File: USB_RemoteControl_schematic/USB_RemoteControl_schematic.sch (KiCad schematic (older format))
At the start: 33 parts, among them J1 USB_A, J2 FOUR_WIRE_CONN, SW1 ~rst, SW2 boot, U1 AMS1117-3.3, U2 STM32F103C6Tx, U3 NRF24L01_Breakout, Y1 8MHz

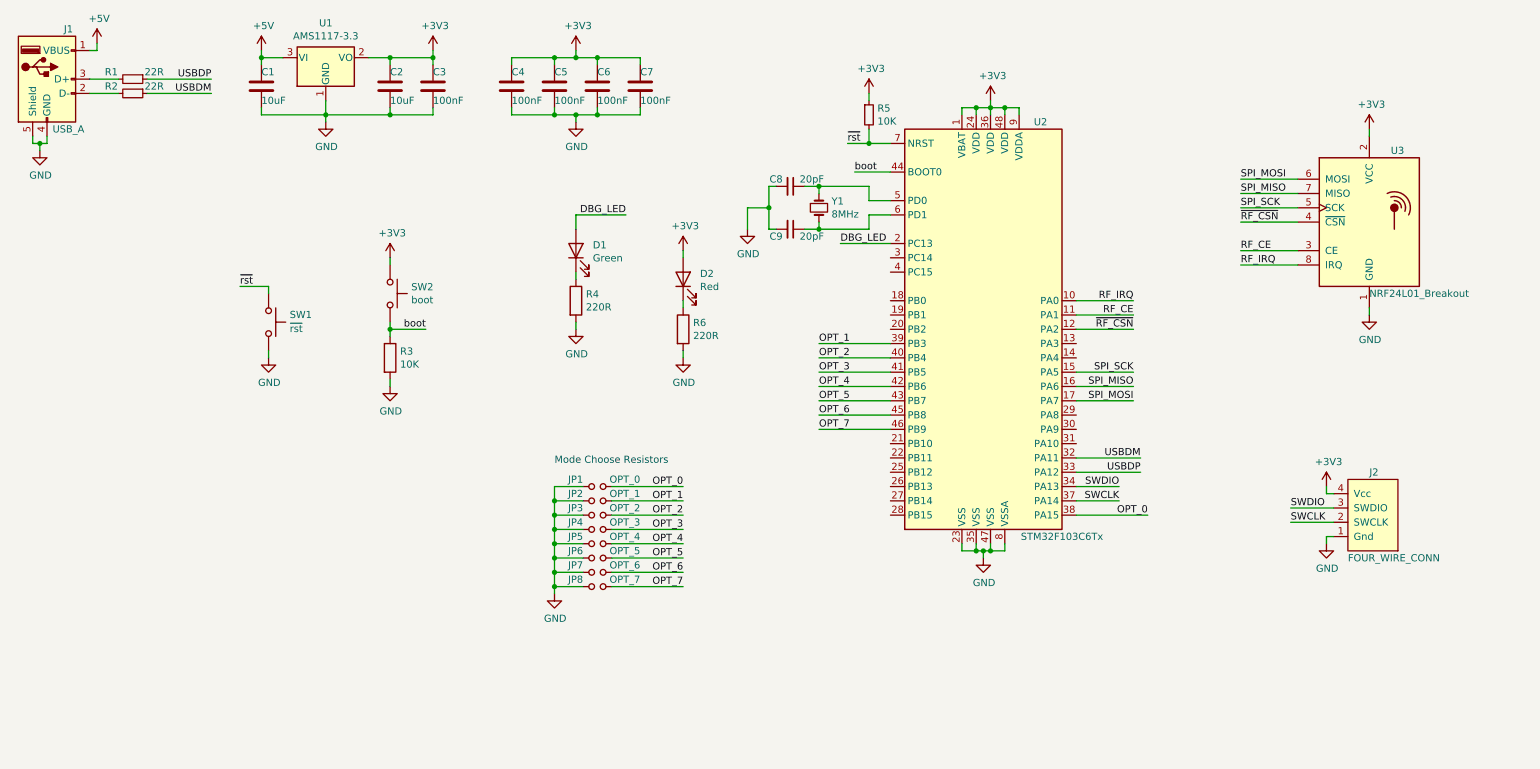
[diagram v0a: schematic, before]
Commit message: Completed schematic for Version02
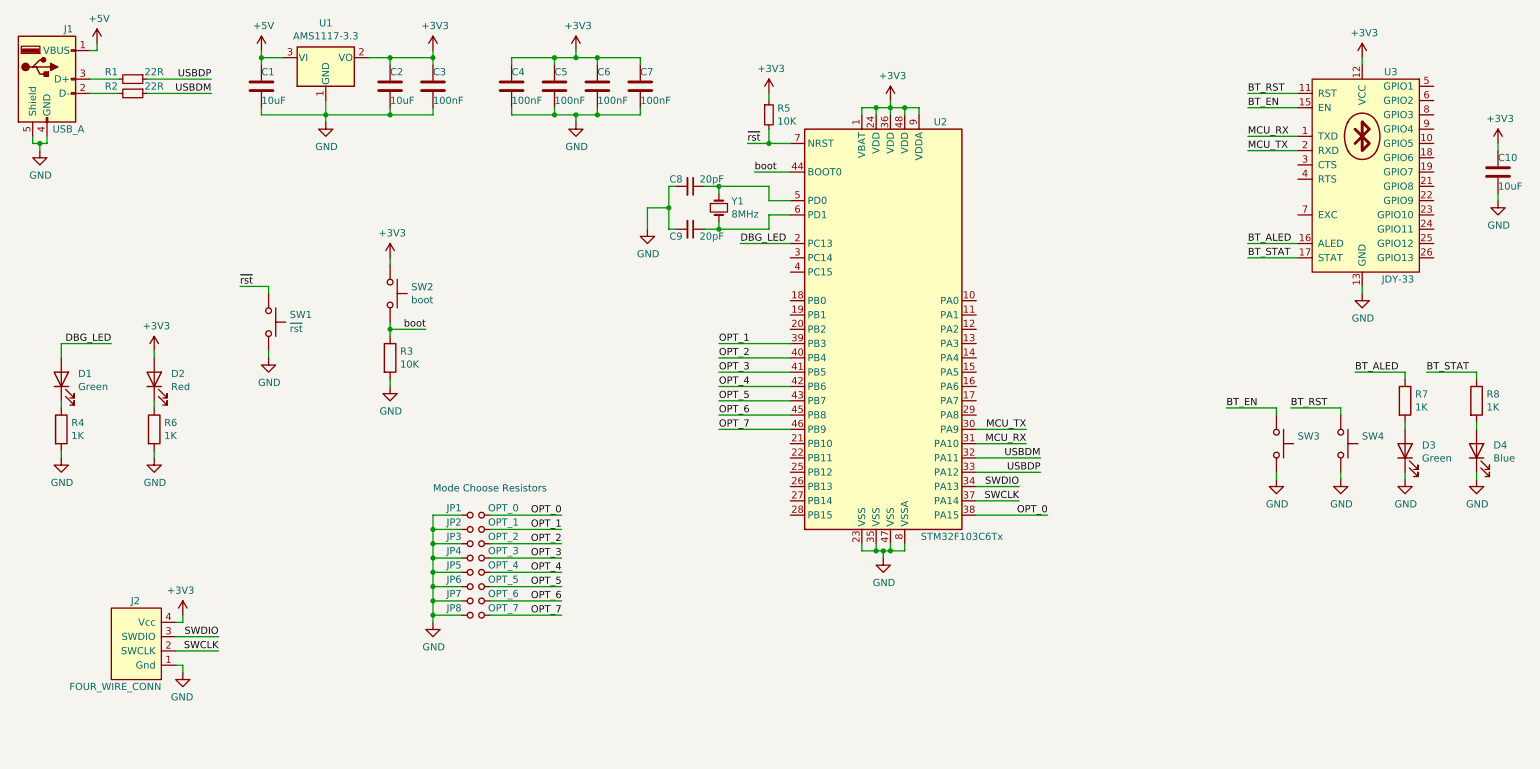
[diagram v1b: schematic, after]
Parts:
- removed U3: NRF24L01_Breakout, RF_Module:nRF24L01_Breakout, symbol RF:NRF24L01_Breakout
- added C10: 10uF, Capacitor_SMD:C_0805_2012Metric_Pad1.18x1.45mm_HandSolder, symbol Device:C
- added D3: Green, LED_SMD:LED_1206_3216Metric_Pad1.42x1.75mm_HandSolder, symbol Device:LED
- added D4: Blue, LED_SMD:LED_1206_3216Metric_Pad1.42x1.75mm_HandSolder, symbol Device:LED
- added R7, R8: 1K, Resistor_SMD:R_0805_2012Metric_Pad1.20x1.40mm_HandSolder, symbol Device:R
- added SW3, SW4: ~, custom_buttons_switches:TSB008, symbol Switch:SW_Push
- added U3: JDY-33, Bluetooth_Custom:JDY-33, JDY-32, JDY-31, JDY-30, JDY-09, symbol Bluetooth_Custom:JDY-33
- C1, C2: footprint Capacitor_SMD:C_1206_3216Metric_Pad1.33x1.80mm_HandSolder -> Capacitor_SMD:C_0805_2012Metric_Pad1.18x1.45mm_HandSolder
- C3, C4, C5, C6, C7: footprint Capacitor_SMD:C_0603_1608Metric_Pad1.08x0.95mm_HandSolder -> Capacitor_SMD:C_0805_2012Metric_Pad1.18x1.45mm_HandSolder
- J1: footprint Connector_USB:USB_A_CONNFLY_DS1095-WNR0 -> Connectors_Custom:USB_A_Male
- R4, R6: value 220R -> 1K
- Y1: footprint Crystal:Crystal_SMD_HC49-SD_HandSoldering -> Crystal:Crystal_SMD_HC49-SD
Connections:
- net +3V3: now also C10.1, U3.12 (VCC)
- net GND: now also C10.2, D3.1 (K), D4.1 (K), SW3.2, SW4.2, U3.13 (GND)
- net MCU_TX: now reaches U2.30 (PA9)
- net MCU_TX: now also U3.2 (RXD)
- net MCU_RX: now reaches U2.31 (PA10)
- net MCU_RX: now also U3.1 (TXD)
- net RF_CE: no longer names the net of U2.11 (PA1)
- net RF_IRQ: no longer names the net of U2.10 (PA0)
- net SPI_MISO: no longer names the net of U2.16 (PA6)
- net SPI_MOSI: no longer names the net of U2.17 (PA7)
- net SPI_SCK: no longer names the net of U2.15 (PA5)
- net ~RF_CSN: no longer names the net of U2.12 (PA2)
- new net: D3.2 (A), R7.2
- new net: D4.2 (A), R8.2
- new net BT_ALED: R7.1, U3.16 (ALED)
- new net BT_EN: SW3.1, U3.15 (EN)
- new net BT_RST: SW4.1, U3.11 (RST)
- new net BT_STAT: R8.1, U3.17 (STAT)
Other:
- moved on the sheet: C8, C9, D1, D2, J2, JP1, JP2, JP3, JP4, JP5, JP6, JP7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

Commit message: Finished PCB
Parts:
- removed C10: 10uF, Capacitor_SMD:C_0805_2012Metric_Pad1.18x1.45mm_HandSolder, symbol Device:C
- removed JP1: OPT_0, Resistor_SMD:R_0805_2012Metric_Pad1.20x1.40mm_HandSolder, symbol Device:Jumper_NO_Small
- removed JP2: OPT_1, Resistor_SMD:R_0805_2012Metric_Pad1.20x1.40mm_HandSolder, symbol Device:Jumper_NO_Small
- removed JP3: OPT_2, Resistor_SMD:R_0805_2012Metric_Pad1.20x1.40mm_HandSolder, symbol Device:Jumper_NO_Small
- removed JP4: OPT_3, Resistor_SMD:R_0805_2012Metric_Pad1.20x1.40mm_HandSolder, symbol Device:Jumper_NO_Small
- removed JP5: OPT_4, Resistor_SMD:R_0805_2012Metric_Pad1.20x1.40mm_HandSolder, symbol Device:Jumper_NO_Small
- removed JP6: OPT_5, Resistor_SMD:R_0805_2012Metric_Pad1.20x1.40mm_HandSolder, symbol Device:Jumper_NO_Small
- removed JP7: OPT_6, Resistor_SMD:R_0805_2012Metric_Pad1.20x1.40mm_HandSolder, symbol Device:Jumper_NO_Small
- removed JP8: OPT_7, Resistor_SMD:R_0805_2012Metric_Pad1.20x1.40mm_HandSolder, symbol Device:Jumper_NO_Small
- removed U1: AMS1117-3.3, Package_TO_SOT_SMD:SOT-223-3_TabPin2, symbol Regulator_Linear:AMS1117-3.3
- added U1: HT7533, Package_TO_SOT_SMD:SOT-89-3, symbol Regulator_Linear:HT75xx-1-SOT89
- C3, C4, C5, C6, C7: footprint Capacitor_SMD:C_0805_2012Metric_Pad1.18x1.45mm_HandSolder -> Capacitor_SMD:C_0603_1608Metric_Pad1.08x0.95mm_HandSolder
- D1, D2, D3, D4: footprint LED_SMD:LED_1206_3216Metric_Pad1.42x1.75mm_HandSolder -> LED_SMD:LED_0805_2012Metric_Pad1.15x1.40mm_HandSolder
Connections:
- net OPT_4 is gone; now on net MCU_TX: U2.42 (PB6)
- net OPT_5 is gone; now on net MCU_RX: U2.43 (PB7)
- net +3V3: now also R6.1, U1.3 (VOUT); no longer D2.2 (A)
- net +5V: now also U1.2 (VIN)
- net DBG_LED: now also R4.1, U2.10 (PA0); no longer D1.2 (A), U2.2 (PC13)
- net GND: now also D1.1 (K), D2.1 (K), U1.1 (GND); no longer R4.2, R6.2
- net MCU_RX: no longer U2.31 (PA10)
- net MCU_TX: no longer U2.30 (PA9)
- net OPT_0: no longer names the net of U2.38 (PA15)
- net OPT_1: no longer names the net of U2.39 (PB3)
- net OPT_2: no longer names the net of U2.40 (PB4)
- net OPT_3: no longer names the net of U2.41 (PB5)
- net OPT_6: no longer names the net of U2.45 (PB8)
- net OPT_7: no longer names the net of U2.46 (PB9)
- new net: D1.2 (A), R4.2
- new net: D2.2 (A), R6.2
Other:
- note removed: "Mode Choose Resistors"
- moved on the sheet: D1, D2, R4, R6

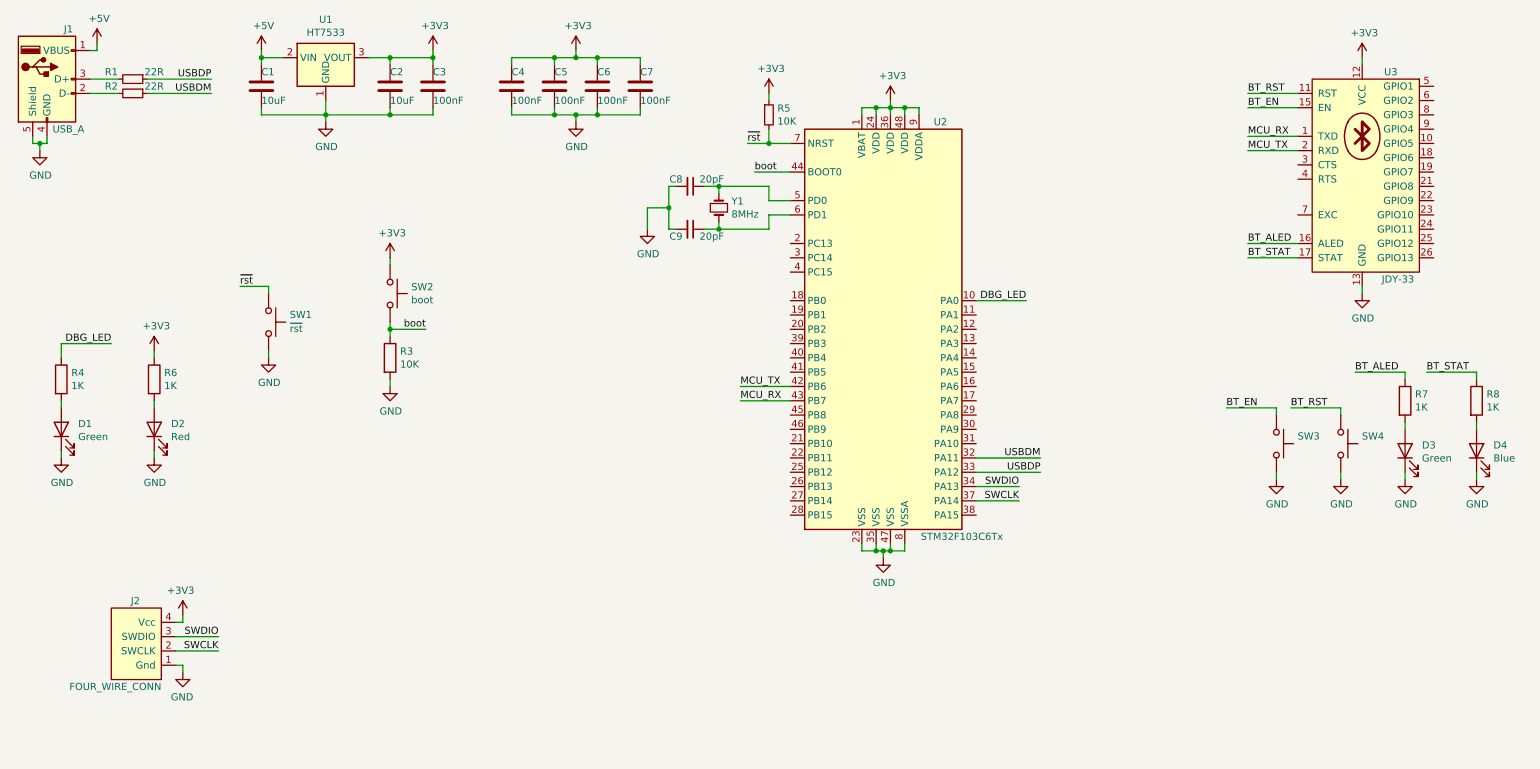
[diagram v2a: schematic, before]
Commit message: Improved readability of the schematic
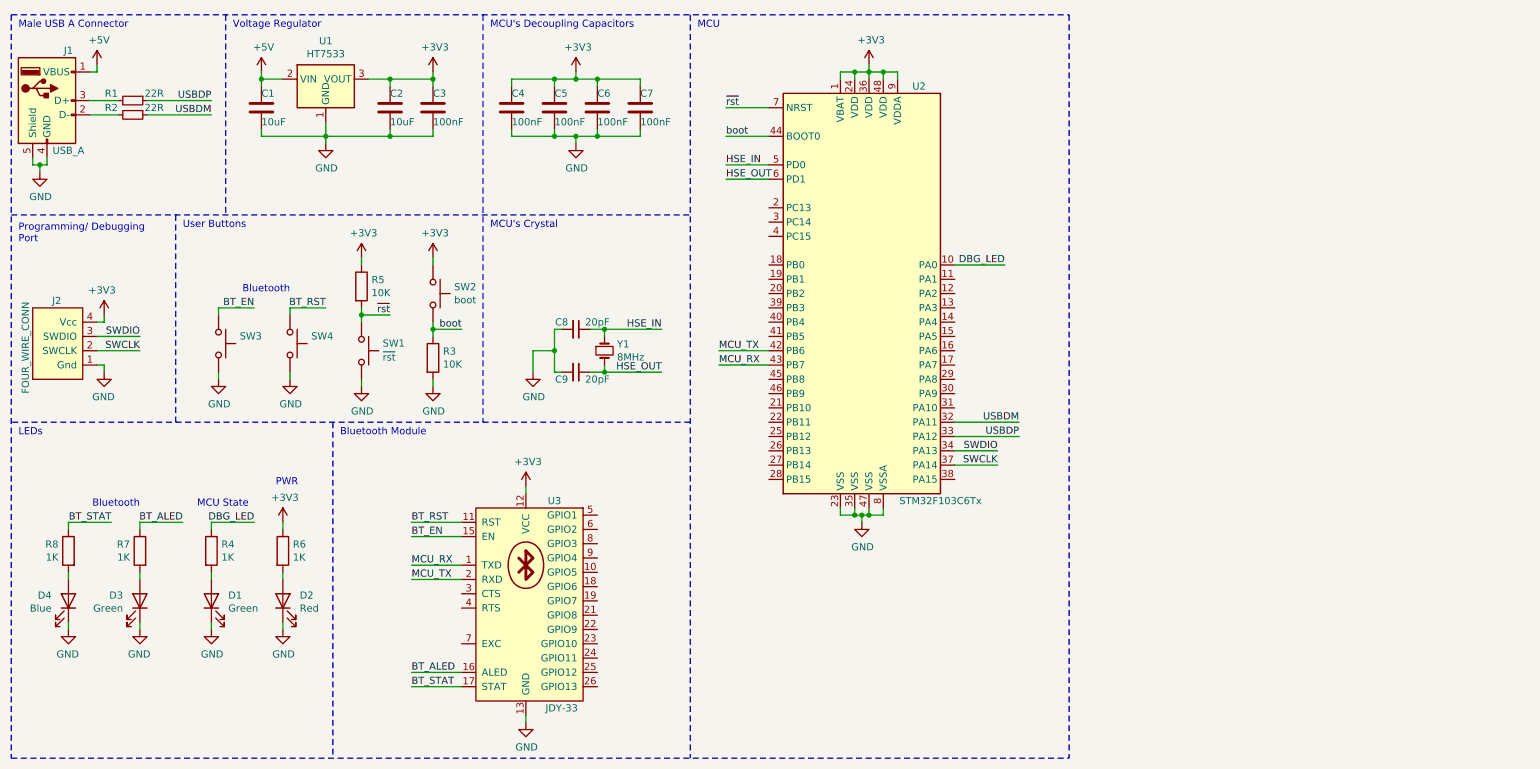
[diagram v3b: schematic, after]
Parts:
- removed R5: 10K, Resistor_SMD:R_0805_2012Metric_Pad1.20x1.40mm_HandSolder, symbol Device:R_Small
- added R5: 10K, Resistor_SMD:R_0805_2012Metric_Pad1.20x1.40mm_HandSolder, symbol Device:R
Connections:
- net +3V3: now also R5.1
- net ~rst: now also R5.2
- net HSE_IN: now reaches C8.1, U2.5 (PD0), Y1.1
- net HSE_OUT: now reaches C9.1, U2.6 (PD1), Y1.2
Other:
- note added: "Bluetooth"
- note added: "Bluetooth Module"
- note added: "LEDs"
- note added: "MCU"
- note added: "MCU State"
- note added: "MCU's Crystal"
- note added: "MCU's Decoupling Capacitors"
- note added: "Male USB A Connector"
- note added: "PWR"
- note added: "Programming/ Debugging \nPort"
- note added: "User Buttons"
- note added: "Voltage Regulator"
- moved on the sheet: C1, C2, C3, C4, C5, C6, C7, C8, C9, D1, D2, D3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
